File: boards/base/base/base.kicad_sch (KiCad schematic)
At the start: 25 parts, among them J1 Conn_01x04_Female, J2 Conn_01x06_Female, J3 Conn_01x06_Female, J4 Screw_Terminal_01x02, J5 Conn_01x03_Female, J6 Conn_01x02_Male, Q1 BC547, Q2 BC547, Q3 2SD1047, Q4 BCP56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

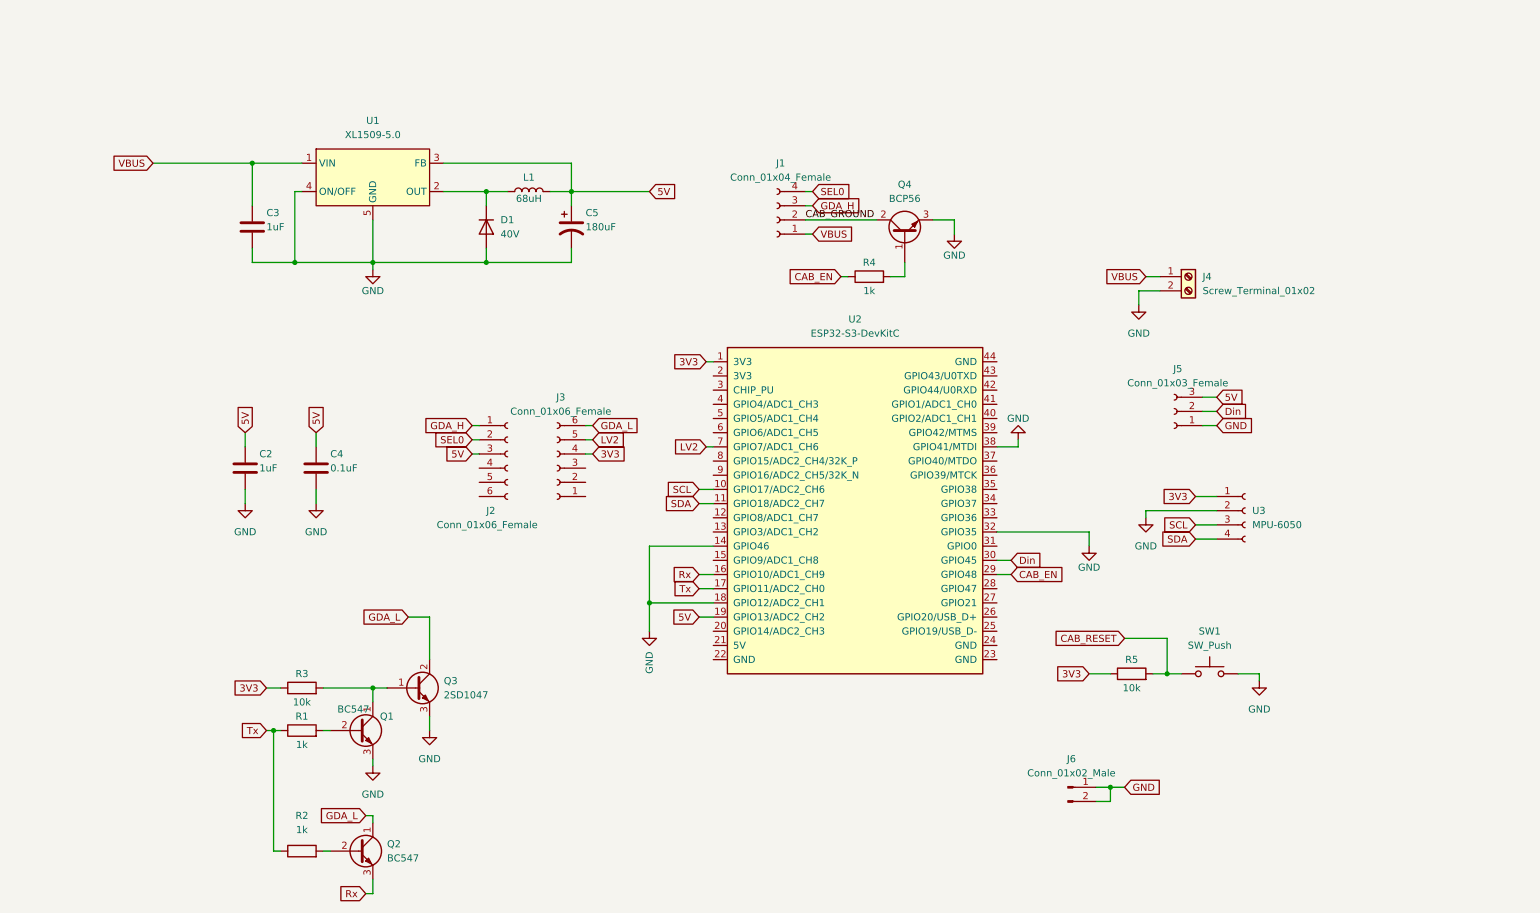
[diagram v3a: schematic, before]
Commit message: Added diode on base
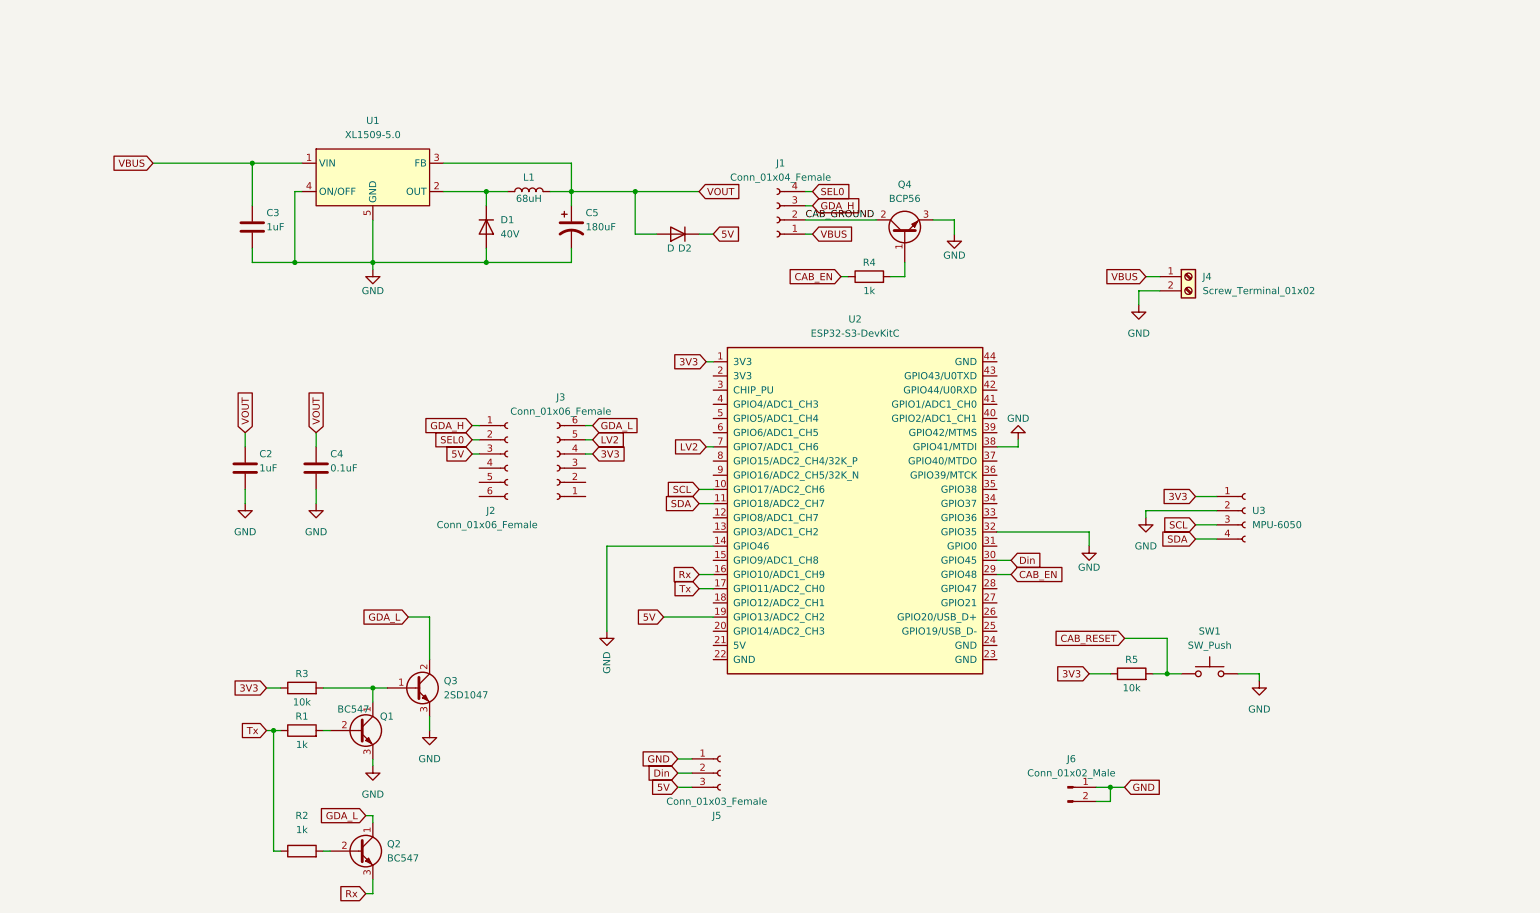
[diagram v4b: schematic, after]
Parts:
- added D2: D, Resistor_THT:R_Box_L8.4mm_W2.5mm_P5.08mm, symbol Device:D
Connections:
- net 5V: now also D2.1 (K); no longer C2.1, C4.1, C5.1, L1.2, U1.3 (FB)
- net GND: no longer U2.18 (GPIO12/ADC2_CH1)
- new net VOUT: C2.1, C4.1, C5.1, D2.2 (A), L1.2, U1.3 (FB)
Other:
- moved on the sheet: J5

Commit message: Tidied Base PCB
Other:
- note added: "Cabinet reset"
- note added: "Connector"
- note added: "ESP32"
- note added: "Level Shifter"
- note added: "MPU6050"
- note added: "Open-drain"
- note added: "Power"
- note added: "WS2812"
- moved on the sheet: C2, C3, C4, C5, D1, D2, J1, J2, J3, J4, J5, J6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

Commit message: Base V2
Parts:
- removed D2: D, Resistor_THT:R_Box_L8.4mm_W2.5mm_P5.08mm, symbol Device:D
- removed Q2: BC547, Package_TO_SOT_THT:TO-92_Inline, symbol Transistor_BJT:BC547
- removed Q3: 2SD1047, Package_TO_SOT_THT:TO-220-3_Vertical, symbol Transistor_BJT:2SD1047
- removed Q4: BCP56, Package_TO_SOT_SMD:TO-263-3_TabPin2, symbol Transistor_BJT:BCP56
- removed R1, R2: 1k, Resistor_THT:R_Axial_DIN0207_L6.3mm_D2.5mm_P10.16mm_Horizontal, symbol Device:R
- removed R3: 10k, Resistor_THT:R_Axial_DIN0207_L6.3mm_D2.5mm_P10.16mm_Horizontal, symbol Device:R
- removed R5: 10k, Resistor_SMD:R_0805_2012Metric, symbol Device:R
- added D3: D, Resistor_THT:R_Box_L8.4mm_W2.5mm_P5.08mm, symbol Device:D
- added J7: Conn_01x02_Female, TerminalBlock_Altech:Altech_AK300_1x02_P5.00mm_45-Degree, symbol Connector:Conn_01x02_Female
- added J8: Conn_01x03_Female, Connector_PinHeader_2.54mm:PinHeader_1x03_P2.54mm_Vertical, symbol Connector:Conn_01x03_Female
- added R6, R7, R8: 100, Resistor_THT:R_Axial_DIN0207_L6.3mm_D2.5mm_P5.08mm_Vertical, symbol Device:R
- R4: value 1k -> 10k; footprint Resistor_SMD:R_0805_2012Metric -> Resistor_THT:R_Axial_DIN0207_L6.3mm_D2.5mm_P5.08mm_Vertical
- SW1: footprint TerminalBlock_4Ucon:TerminalBlock_4Ucon_1x02_P3.50mm_Vertical -> Connector_PinHeader_2.54mm:PinHeader_1x02_P2.54mm_Vertical
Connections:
- net VOUT is gone; now on net 5V: C2.1, C4.1, C5.1, L1.2, U1.3 (FB)
- net 5V: now also J8.2 (Pin_2)
- net CAB_EN: now also J8.3 (Pin_3); no longer R4.1
- net CAB_GROUND: now also J7.2 (Pin_2)
- net CAB_RESET: now also U2.37 (GPIO40/MTDO)
- net GDA_H: now also R7.1; no longer J2.1 (Pin_1)
- net GDA_L: now also Q1.3 (E), D3.2 (A)
- net GND: now also J2.4 (Pin_4), J3.3 (Pin_3), J7.1 (Pin_1), J8.1 (Pin_1); no longer Q1.3 (E)
- net Rx: now also U2.13 (GPIO3/ADC1_CH2), R6.2; no longer U2.16 (GPIO10/ADC1_CH9)
- net SEL0: now also R8.1; no longer J2.2 (Pin_2)
- net Tx: now also R4.1, U2.15 (GPIO9/ADC1_CH8), D3.1 (K); no longer U2.17 (GPIO11/ADC2_CH0)
- net at Q1.1 (C): now also R6.1
- net at Q1.2 (B): now also R4.2
- new net: J2.1 (Pin_1), R7.2
- new net: J2.2 (Pin_2), R8.2
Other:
- moved on the sheet: J2, J3
